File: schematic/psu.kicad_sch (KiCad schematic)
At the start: 6 parts, among them J1 Barrel_Jack_Switch, SW1 SW_Push, SW2 SW_SPDT

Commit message: added volume and adjusted cart port
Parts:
- SW1: footprint Button_Switch_THT:SW_PUSH_6mm -> Button_Switch_THT:SW_Tactile_SKHH_Angled
- SW2: footprint Button_Switch_THT:SW_CuK_OS102011MA1QN1_SPDT_Angled -> 1101M2S3ABE2:1101M2S3ABE2
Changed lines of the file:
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@@
       (effects (font (size 1.27 1.27)) (justify left))
     )
-    (property "Footprint" "Button_Switch_THT:SW_PUSH_6mm" (at 144.907 96.52 0)
+    (property "Footprint" "Button_Switch_THT:SW_Tactile_SKHH_Angled" (at 144.907 96.52 0)
       (effects (font (size 1.27 1.27)) hide)
     )
@@
       (effects (font (size 1.27 1.27)))
     )
-    (property "Footprint" "Button_Switch_THT:SW_CuK_OS102011MA1QN1_SPDT_Angled" (at 124.714 94.234 0)
+    (property "Footprint" "1101M2S3ABE2:1101M2S3ABE2" (at 124.714 94.234 0)
       (effects (font (size 1.27 1.27)) hide)
     )

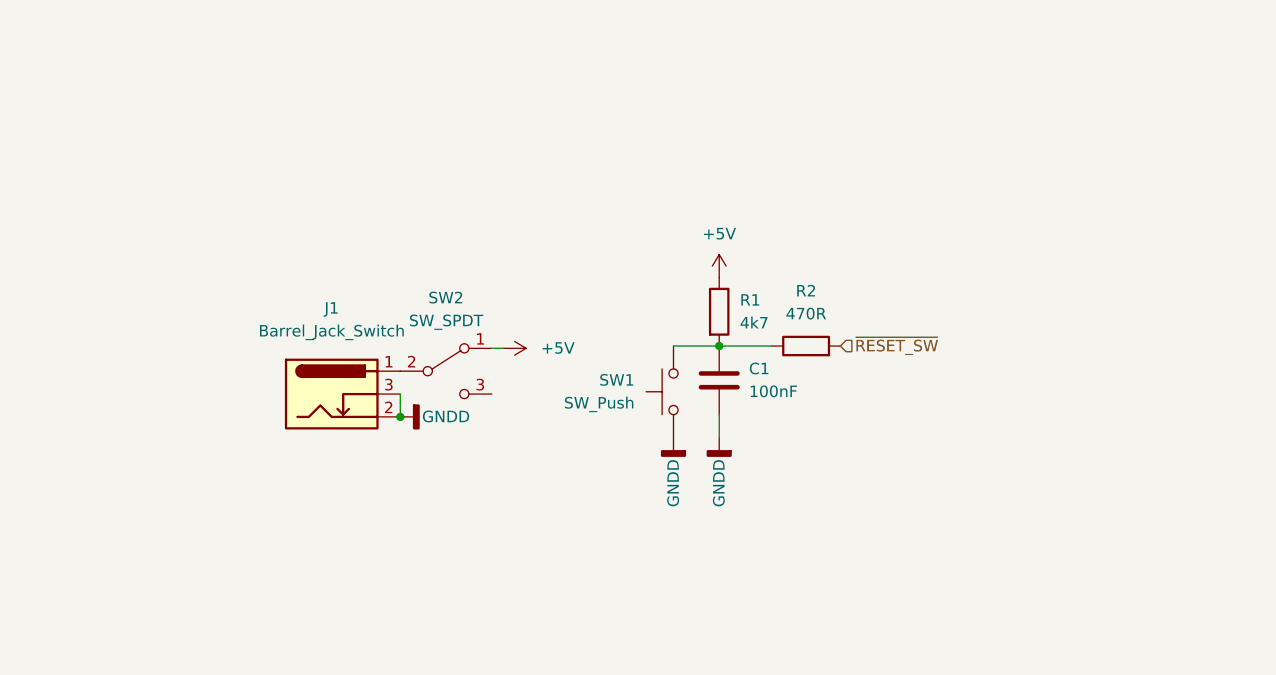
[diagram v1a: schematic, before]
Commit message: first iteration of version v1. PCB placed, checked but needs final go through and case design before send out.
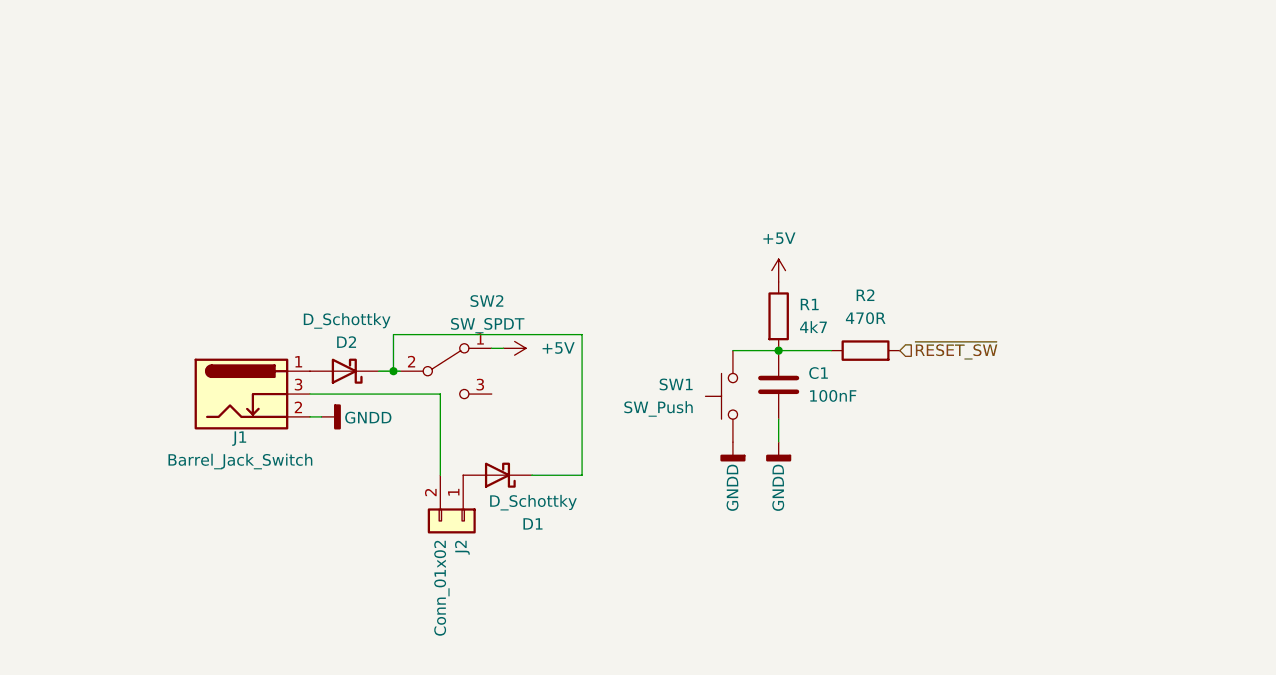
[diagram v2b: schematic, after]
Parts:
- added D1, D2: D_Schottky, Diode_THT:D_DO-41_SOD81_P3.81mm_Vertical_AnodeUp, symbol Device:D_Schottky
- added J2: Conn_01x02, Connector_Molex:Molex_KK-254_AE-6410-02A_1x02_P2.54mm_Vertical, symbol Connector_Generic:Conn_01x02
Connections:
- net GNDD: no longer J1.3
- net at SW2.2 (B): now also D1.1 (K), D2.1 (K); no longer J1.1
- new net: D2.2 (A), J1.1
- new net: J1.3, J2.2 (Pin_2)
- new net: D1.2 (A), J2.1 (Pin_1)
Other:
- moved on the sheet: C1, J1, R1, R2, SW1

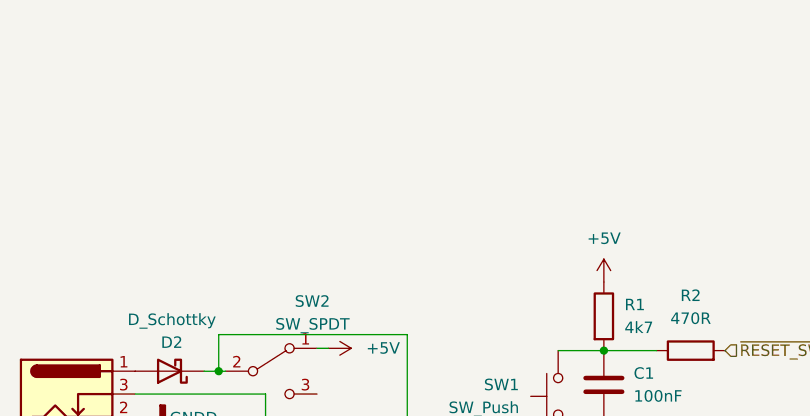
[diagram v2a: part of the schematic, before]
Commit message: added power port for lcd and adjusted board traces and fill
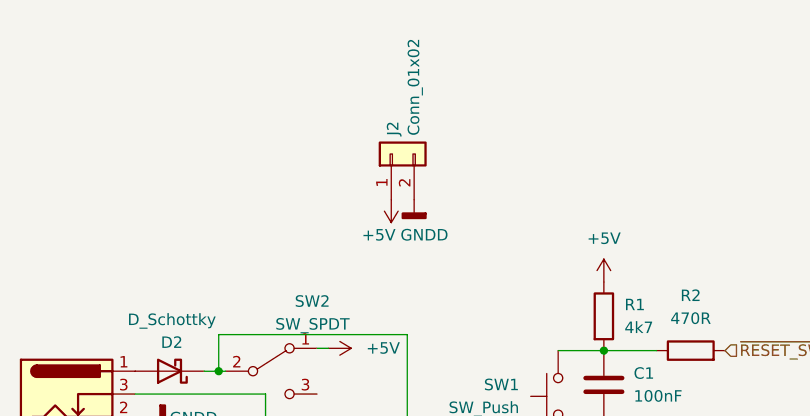
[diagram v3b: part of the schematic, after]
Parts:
- added J2: Conn_01x02, Connector_Molex:Molex_KK-254_AE-6410-02A_1x02_P2.54mm_Vertical, symbol Connector_Generic:Conn_01x02
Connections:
- net +5V: now also J2.1 (Pin_1)
- net GNDD: now also J2.2 (Pin_2)
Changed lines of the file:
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@@
+    )
+  )
+  (symbol (lib_id "power:GNDD") (at 140.589 75.184 0) (mirror y) (unit 1)
+    (in_bom yes) (on_board yes) (dnp no)
+    (property "Reference" "#PWR02" (at 140.589 81.534 0)
+      (effects (font (size 1.27 1.27)) hide)
+    )
+    (property "Value" "GNDD" (at 141.732 79.121 0)
+      (effects (font (size 1.27 1.27)))
+    )
+    (property "Footprint" "" (at 140.589 75.184 0)
+      (effects (font (size 1.27 1.27)) hide)
+    )
+    (property "Datasheet" "" (at 140.589 75.184 0)
+      (effects (font (size 1.27 1.27)) hide)
+    )
+    (pin "1")
+    (instances
+      (project "coleco_original"
+        (path "/970e0f64-111f-41e3-9f5a-fb0d0f6fa101/00000000-0000-0000-0000-000062624797"
+          (reference "#PWR02") (unit 1)
+        )
+      )
+    )
+  )
+  (symbol (lib_id "Connector_Generic:Conn_01x02") (at 138.049 70.104 90) (unit 1)
+    (in_bom yes) (on_board yes) (dnp no)
+    (property "Reference" "J2" (at 138.2522 68.072 0)
+      (effects (font (size 1.27 1.27)) (justify left))
+    )
+    (property "Value" "Conn_01x02" (at 140.5636 68.072 0)
+      (effects (font (size 1.27 1.27)) (justify left))
+    )
+    (property "Footprint" "Connector_Molex:Molex_KK-254_AE-6410-02A_1x02_P2.54mm_Vertical" (at 138.049 70.104 0)
+      (effects (font (size 1.27 1.27)) hide)
+    )
+    (property "Datasheet" "~" (at 138.049 70.104 0)
+      (effects (font (size 1.27 1.27)) hide)
+    )
+    (pin "1")
+    (pin "2")
+    (instances
+      (project "coleco_original"
+        (path "/970e0f64-111f-41e3-9f5a-fb0d0f6fa101/00000000-0000-0000-0000-000062624749"
+          (reference "J2") (unit 1)
+        )
+        (path "/970e0f64-111f-41e3-9f5a-fb0d0f6fa101"
+          (reference "J9") (unit 1)
+        )
+        (path "/970e0f64-111f-41e3-9f5a-fb0d0f6fa101/00000000-0000-0000-0000-000062624797"
+          (reference "J11") (unit 1)
+        )
+      )
+      (project "picerino_sn76489AN"
+        (path "/b5352a33-563a-4ffe-a231-2e68fb54afa3"
+          (reference "J2") (unit 1)
+        )
+      )
     )
   )
@@
         )
       )
+    )
+  )
+  (symbol (lib_id "power:+5V") (at 138.049 75.184 180) (unit 1)
+    (in_bom yes) (on_board yes) (dnp no)
+    (property "Reference" "#PWR01" (at 138.049 71.374 0)
+      (effects (font (size 1.27 1.27)) hide)
+    )
+    (property "Value" "+5V" (at 136.652 79.121 0)
+      (effects (font (size 1.27 1.27)))
+    )
+    (property "Footprint" "" (at 138.049 75.184 0)
+      (effects (font (size 1.27 1.27)) hide)
+    )
+    (property "Datasheet" "" (at 138.049 75.184 0)
+      (effects (font (size 1.27 1.27)) hide)
+    )
+    (pin "1")
+    (instances
+      (project "coleco_original"
+        (path "/970e0f64-111f-41e3-9f5a-fb0d0f6fa101/00000000-0000-0000-0000-000062624797"
+          (reference "#PWR01") (unit 1)
+        )
+      )

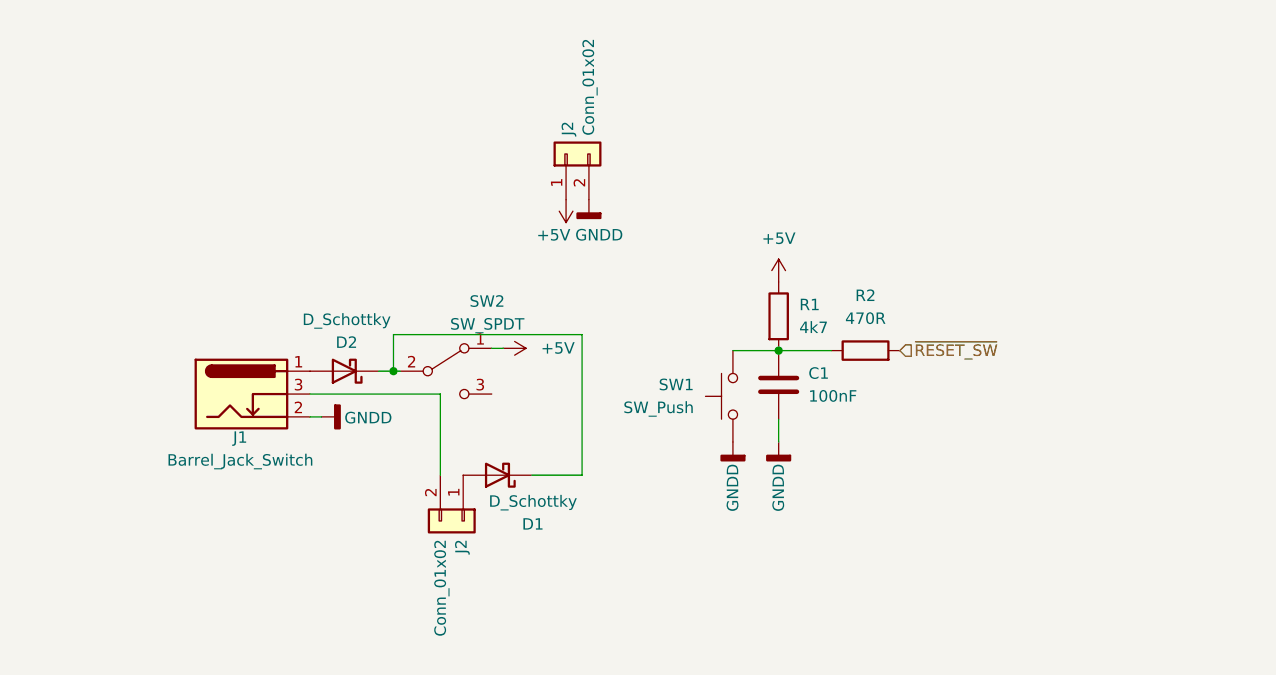
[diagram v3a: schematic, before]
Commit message: first version with roller controller compat
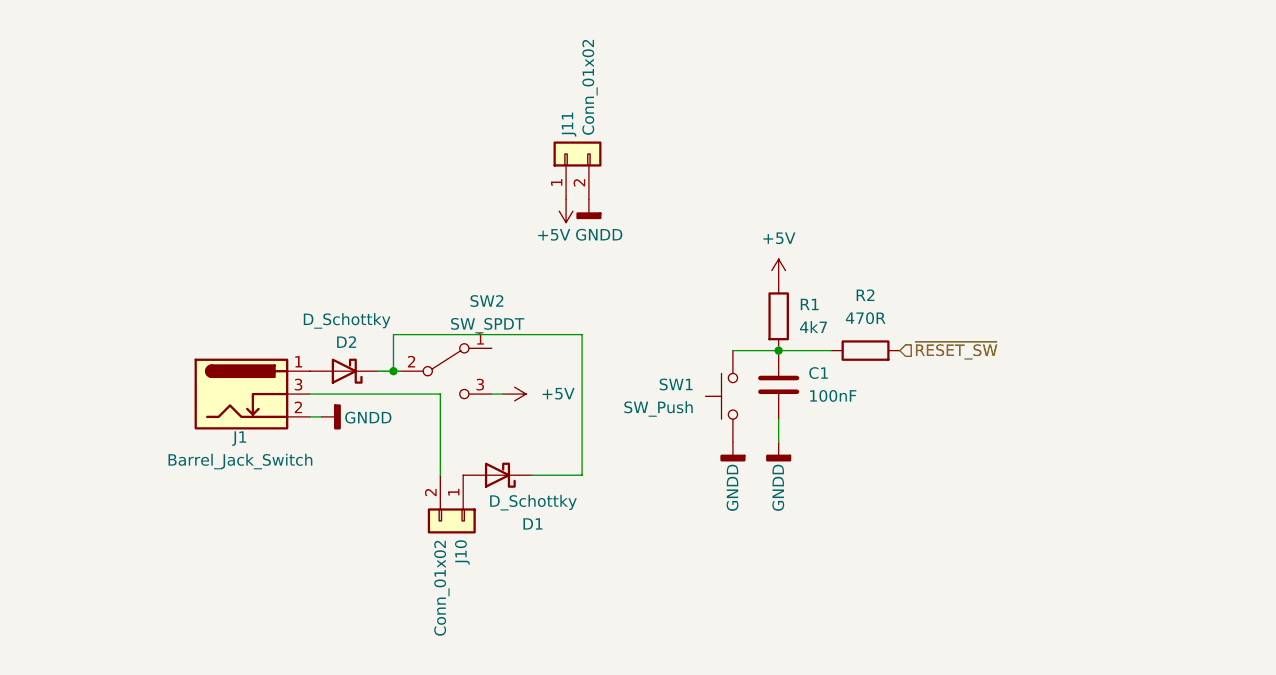
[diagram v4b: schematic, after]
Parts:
- renumbered J2 to J10, J2 to J11
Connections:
- net +5V: now also SW2.3 (C); no longer SW2.1 (A)
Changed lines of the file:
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@@
     (stroke (width 0) (type default))
   )
-  (wire (pts (xy 129.794 91.694) (xy 131.064 91.694))
+  (wire (pts (xy 129.794 96.774) (xy 131.064 96.774))
     (stroke (width 0) (type default))
   )
@@
   (symbol (lib_id "Connector_Generic:Conn_01x02") (at 138.049 70.104 90) (unit 1)
     (in_bom yes) (on_board yes) (dnp no)
-    (property "Reference" "J2" (at 138.2522 68.072 0)
+    (property "Reference" "J11" (at 138.2522 68.072 0)
       (effects (font (size 1.27 1.27)) (justify left))
     )
@@
     (instances
       (project "coleco_original"
-        (path "/970e0f64-111f-41e3-9f5a-fb0d0f6fa101/00000000-0000-0000-0000-000062624749"
-          (reference "J2") (unit 1)
-        )
-        (path "/970e0f64-111f-41e3-9f5a-fb0d0f6fa101"
-          (reference "J9") (unit 1)
-        )
         (path "/970e0f64-111f-41e3-9f5a-fb0d0f6fa101/00000000-0000-0000-0000-000062624797"
           (reference "J11") (unit 1)
@@
     )
   )
-  (symbol (lib_id "power:+5V") (at 131.064 91.694 270) (unit 1)
+  (symbol (lib_id "power:+5V") (at 131.064 96.774 270) (unit 1)
     (in_bom yes) (on_board yes) (dnp no) (fields_autoplaced)
-    (property "Reference" "#PWR06" (at 127.254 91.694 0)
-      (effects (font (size 1.27 1.27)) hide)
-    )
-    (property "Value" "+5V" (at 135.255 91.694 90)
-      (effects (font (size 1.27 1.27)) (justify left))
-    )
-    (property "Footprint" "" (at 131.064 91.694 0)
-      (effects (font (size 1.27 1.27)) hide)
-    )
-    (property "Datasheet" "" (at 131.064 91.694 0)
+    (property "Reference" "#PWR06" (at 127.254 96.774 0)
+      (effects (font (size 1.27 1.27)) hide)
+    )
+    (property "Value" "+5V" (at 135.255 96.774 90)
+      (effects (font (size 1.27 1.27)) (justify left))
+    )
+    (property "Footprint" "" (at 131.064 96.774 0)
+      (effects (font (size 1.27 1.27)) hide)
+    )
+    (property "Datasheet" "" (at 131.064 96.774 0)
       (effects (font (size 1.27 1.27)) hide)
     )
@@
   (symbol (lib_id "Connector_Generic:Conn_01x02") (at 126.619 110.871 270) (unit 1)
     (in_bom yes) (on_board yes) (dnp no)
-    (property "Reference" "J2" (at 126.4158 112.903 0)
+    (property "Reference" "J10" (at 126.4158 112.903 0)
       (effects (font (size 1.27 1.27)) (justify left))
     )
@@
     (instances
       (project "coleco_original"
-        (path "/970e0f64-111f-41e3-9f5a-fb0d0f6fa101/00000000-0000-0000-0000-000062624749"
-          (reference "J2") (unit 1)
-        )
-        (path "/970e0f64-111f-41e3-9f5a-fb0d0f6fa101"
-          (reference "J9") (unit 1)
-        )
         (path "/970e0f64-111f-41e3-9f5a-fb0d0f6fa101/00000000-0000-0000-0000-000062624797"
           (reference "J10") (unit 1)

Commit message: update pdf schematic and schematic wording
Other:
- title: Righteous Tentacle, Colecovision Reverse Engineering Project -> Mini Colecovision
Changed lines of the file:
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@@
   (paper "USLetter")
   (title_block
-    (title "Righteous Tentacle, Colecovision Reverse Engineering Project")
-    (date "2023-06-18")
-    (rev "1.0.0.F")
+    (title "Mini Colecovision")
+    (date "2024-03-25")
+    (rev "1.0.0")
     (company "sparkletron")
     (comment 1 "Jay Convertino")
     (comment 2 "MIT LICENSE")
-    (comment 3 "PCB: 75743 REV F")
+    (comment 3 "TARGET: Portable")
   )
   (junction (at 161.671 91.948) (diameter 0) (color 0 0 0 0)

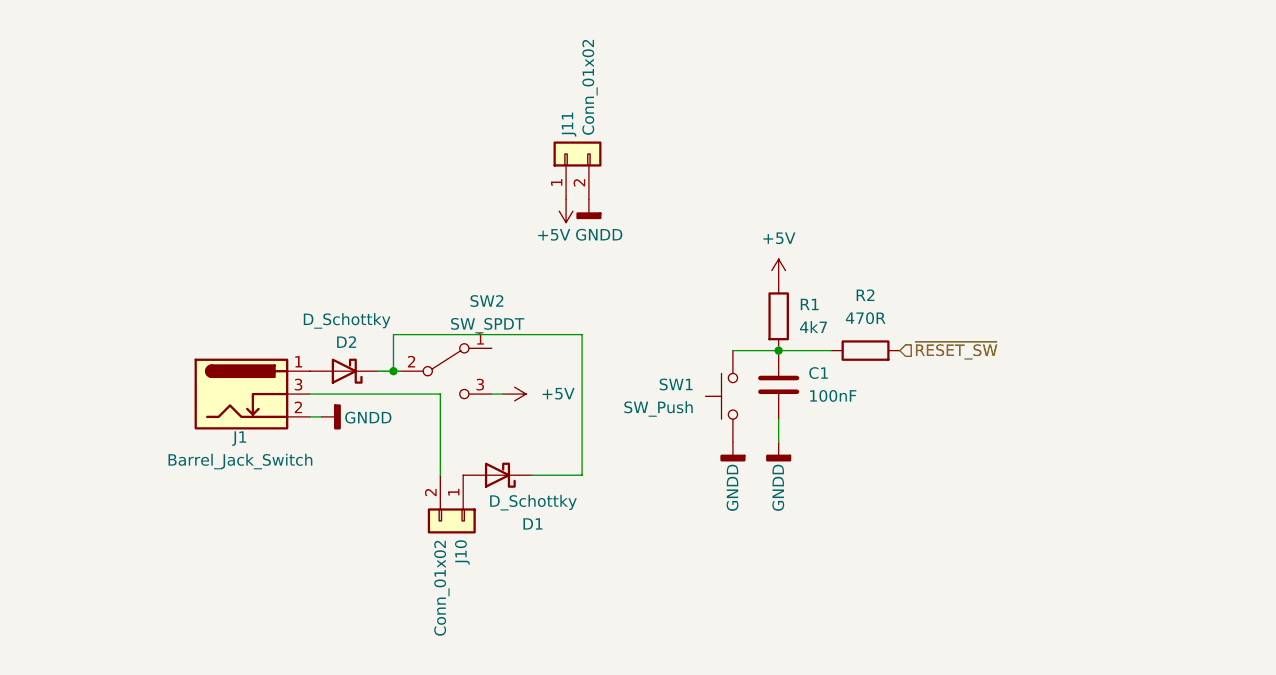
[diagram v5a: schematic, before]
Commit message: first commit with PCB revised for super game module. Needs model updates and tweaks
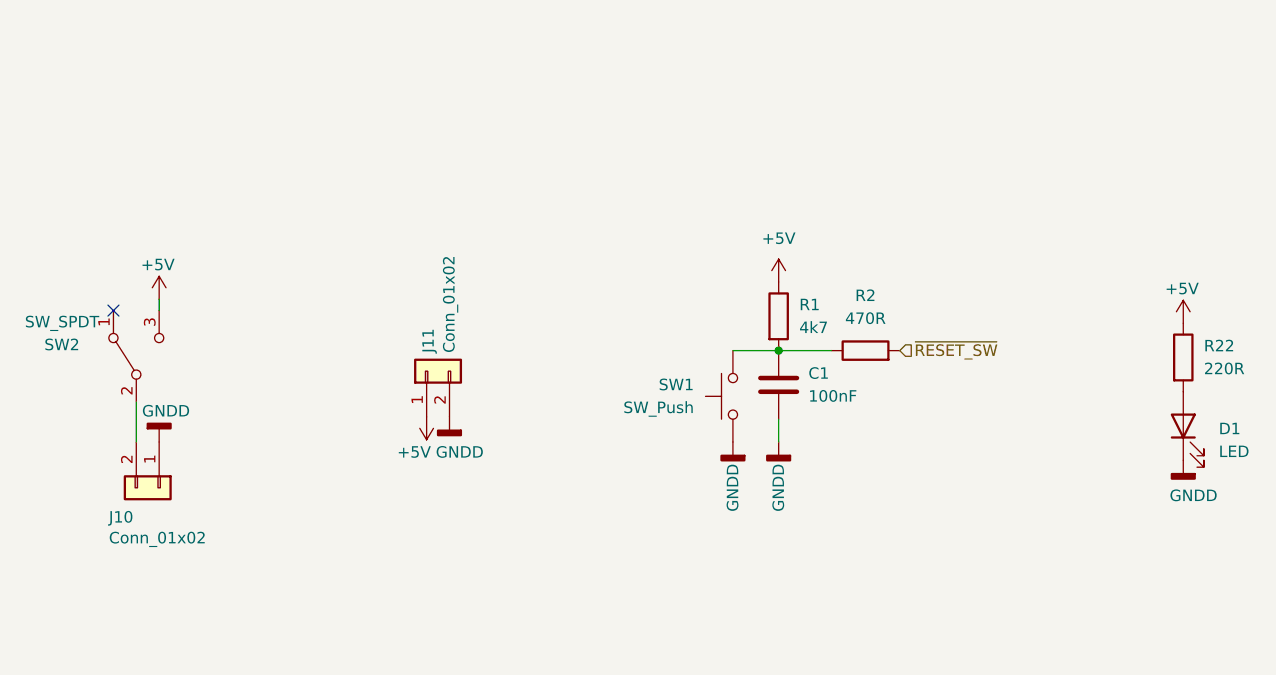
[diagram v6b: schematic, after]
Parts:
- removed D1, D2: D_Schottky, Diode_THT:D_DO-41_SOD81_P3.81mm_Vertical_AnodeUp, symbol Device:D_Schottky
- removed J1: Barrel_Jack_Switch, Connector_BarrelJack:BarrelJack_Horizontal, symbol Connector:Barrel_Jack_Switch
- added D1: LED, LED_THT:LED_D3.0mm, symbol Device:LED
- added R22: 220R, Resistor_THT:R_Axial_DIN0207_L6.3mm_D2.5mm_P10.16mm_Horizontal, symbol Device:R
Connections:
- net +5V: now also R22.1
- net GNDD: now also J10.1 (Pin_1), D1.1 (K)
- net at SW2.2 (B): now also J10.2 (Pin_2)
- new net: D1.2 (A), R22.2
- no-connect marks 0 -> 1
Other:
- moved on the sheet: J10, J11, SW2
